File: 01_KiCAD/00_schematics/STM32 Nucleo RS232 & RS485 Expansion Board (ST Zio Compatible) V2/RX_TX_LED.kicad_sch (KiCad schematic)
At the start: 1 part

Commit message: Removed LED
LED verwijderd dat gebruikt werd voor GitHub Test
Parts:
- removed D1: LED, PCM_SparkFun-LED:LED_0603_1608Metric, symbol PCM_SparkFun-LED:LED
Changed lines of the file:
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@@
 		(comment 3 "Initial revision")
 	)
-	(symbol
-		(lib_id "PCM_SparkFun-LED:LED")
-		(at 73.66 67.31 90)
-		(unit 1)
-		(exclude_from_sim no)
-		(in_bom yes)
-		(on_board yes)
-		(dnp no)
-		(fields_autoplaced yes)
-		(property "Reference" "D1"
-			(at 76.2 65.9764 90)
-			(effects
-				(font
-					(size 1.27 1.27)
-				)
-				(justify right)
-			)
-		)
-		(property "Value" "LED"
-			(at 76.2 68.5164 90)
-			(effects
-				(font
-					(size 1.27 1.27)
-				)
-				(justify right)
-			)
-		)
-		(property "Footprint" "PCM_SparkFun-LED:LED_0603_1608Metric"
-			(at 78.74 67.31 0)
-			(effects
-				(font
-					(size 1.27 1.27)
-				)
-				(hide yes)
-			)
-		)
-		(property "Datasheet" "~"
-			(at 81.28 67.31 0)
-			(effects
-				(font
-					(size 1.27 1.27)
-				)
-				(hide yes)
-			)
-		)
-		(property "Description" "Light emitting diode"
-			(at 86.36 67.31 0)
-			(effects
-				(font
-					(size 1.27 1.27)
-				)
-				(hide yes)
-			)
-		)
-		(property "PROD_ID" "LED-"
-			(at 83.82 67.31 0)
-			(effects
-				(font
-					(size 1.27 1.27)
-				)
-				(hide yes)
-			)
-		)
-		(pin "1"
-		)
-		(pin "2"
-		)
-		(instances
-			(project ""
-				(path "/080f83b7-8913-48e8-ab8e-79cb12295542/d1bb9d55-41f4-4fc3-ae06-1adc98dc5d39"
-					(reference "D1")
-					(unit 1)
-				)
-			)
-		)
-	)
 )

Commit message: Added SHDN logic
Added the SHDN pin logic to have both hardware control and software control vor activating the THVD4431
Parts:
- added C10, C9: 100nF, PCM_SparkFun-Capacitor:C_0603_1608Metric, symbol PCM_SparkFun-Capacitor:0.1uF_0603_25V_20%
- added D2: 1N4148W, Diode_SMD:D_SOD-123, symbol Diode:1N4148W
- added R8: 1K, PCM_fab:R_0603, symbol PCM_fab:R_0603
- added R9: 100K, PCM_fab:R_0603, symbol PCM_fab:R_0603
- added U2: SN74LVC1G14DRL, Package_TO_SOT_SMD:SOT-553, symbol 74xGxx:SN74LVC1G14DRL
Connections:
- new net: D2.1 (K), R8.2
- new net GND: C10.2, C9.2, U2.3 (GND)
- new net L3-TXD: R8.1
- new net TX_RC: C10.1, C9.1, D2.2 (A), R9.2, U2.2
- new net VIO: R9.1

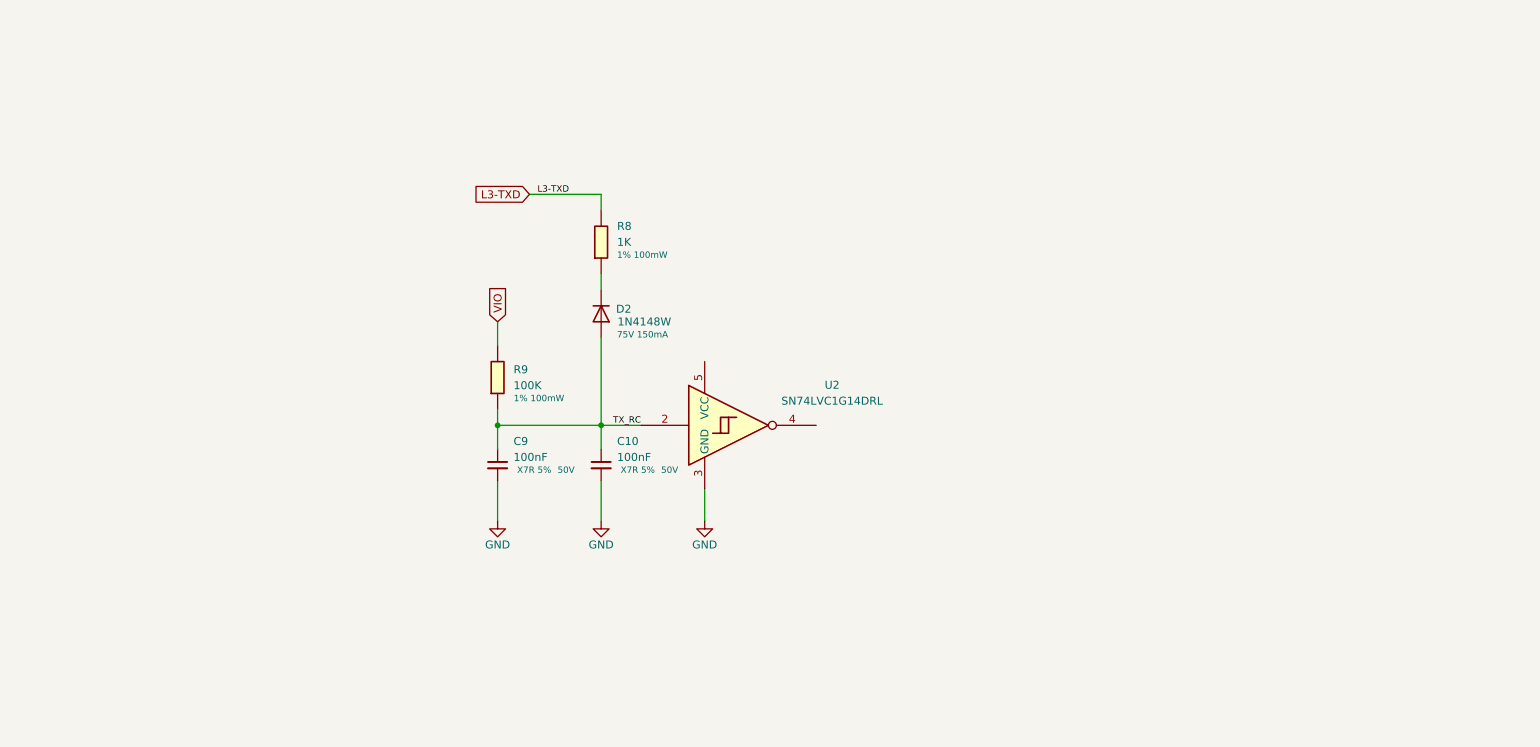
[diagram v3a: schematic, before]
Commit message: Added components and change device
Added dual Schmidt trigger input SN74LVC2G14DBV for LED Rx and Tx control.
Changed sn74hcs245 for alternate part sn74lvc245a for larger footprint and better availability with LCSC.
Difference is sn74lvc245a has no Schmidt-trigger inputs but instead just normal inputs. Fot details see dataseet. Both devices use exact same pin number and configuration except sn74lvc245a has no thermal pad or exposed pad like the sn74hcs245 has.
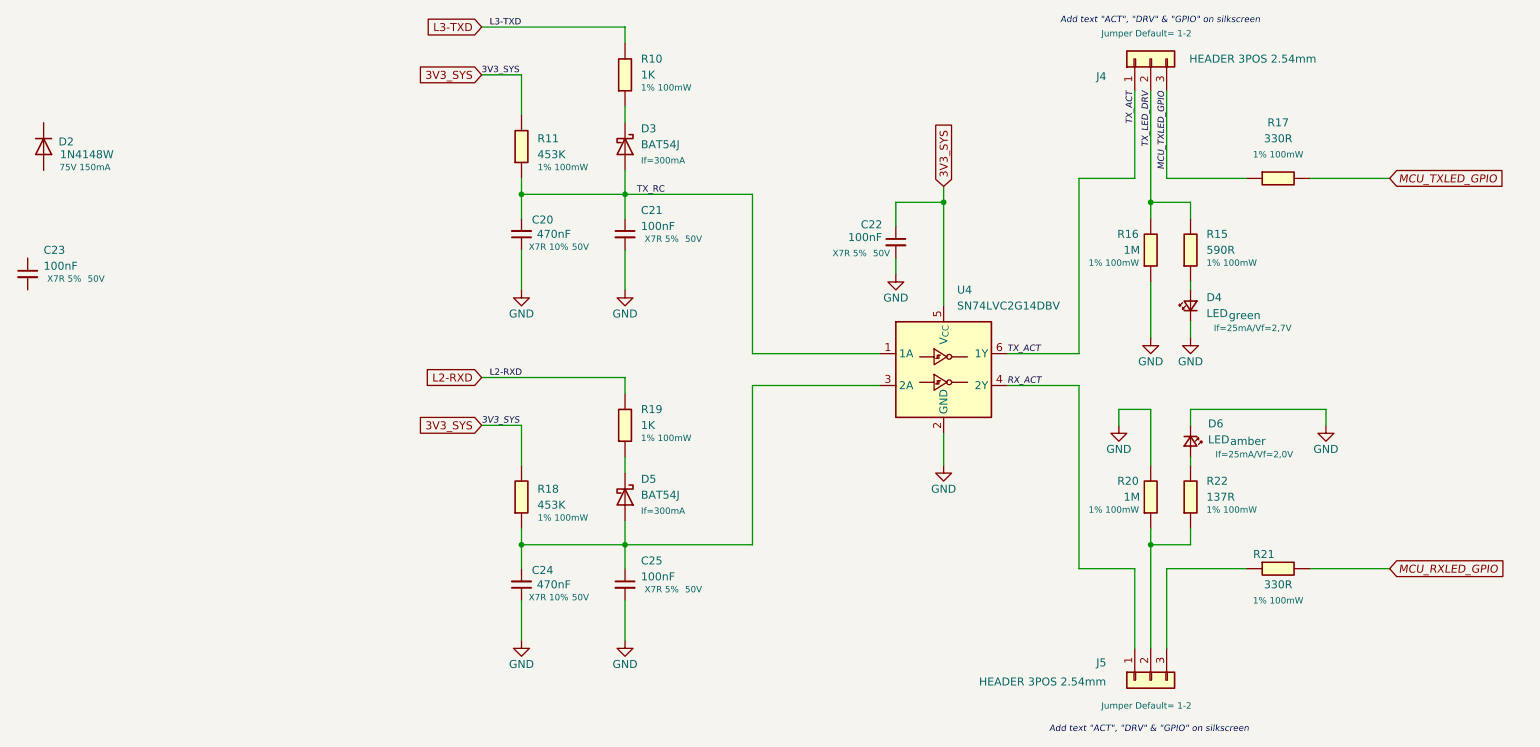
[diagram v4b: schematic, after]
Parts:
- removed U2: SN74LVC1G14DRL, Package_TO_SOT_SMD:SOT-553, symbol 74xGxx:SN74LVC1G14DRL
- added C20, C24: 470nF, PCM_SparkFun-Capacitor:C_0603_1608Metric, symbol PCM_SparkFun-Capacitor:0.1uF_0603_25V_20%
- added C22, C25: 100nF, PCM_SparkFun-Capacitor:C_0603_1608Metric, symbol PCM_SparkFun-Capacitor:0.1uF_0603_25V_20%
- added D3, D5: BAT54J, Diode_SMD:D_SOD-323F, symbol Diode:BAT54J
- added D4, D6: LED, IN-S63AT:LED_0603_WRE, symbol PCM_SparkFun-LED:LED
- added J4, J5: HEADER 3POS 2.54mm, symbol Connector_Generic:Conn_01x03
- added R15: 590R, PCM_fab:R_0603, symbol PCM_fab:R_0603
- added R16, R20: 1M, PCM_fab:R_0603, symbol PCM_fab:R_0603
- added R17, R21: 330R, PCM_fab:R_0603, symbol PCM_fab:R_0603
- added R18: 453K, PCM_fab:R_0603, symbol PCM_fab:R_0603
- added R19: 1K, PCM_fab:R_0603, symbol PCM_fab:R_0603
- added R22: 137R, PCM_fab:R_0603, symbol PCM_fab:R_0603
- added U4: SN74LVC2G14DBV, Package_TO_SOT_SMD:SOT-23-6, symbol 74xGxx:SN74LVC2G14DBV
- R11: renamed from R9; value 100K -> 453K; LCSC C14675 -> C114660; MPN RC0603FR-07100KL -> RC0603FR-07150KL
- renumbered C10 to C21, C9 to C23, R8 to R10
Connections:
- net GND: now also C20.1, C22.2, C24.1, C25.2, D4.1 (K), D6.1 (K), R16.2, R20.1, U4.2 (GND); no longer C23.2
- net TX_RC: now also C20.2, D3.2 (A), U4.1 (1A); no longer C23.1, D2.2 (A)
- net at R10.2: now also D3.1 (K); no longer D2.1 (K)
- net VIO renamed 3V3_SYS
- net 3V3_SYS: now also C22.1, R18.1, U4.5 (V_{CC})
- new net: J5.3 (Pin_3), R21.2
- new net: D5.1 (K), R19.2
- new net: D6.2 (A), R22.1
- new net: C24.2, C25.1, D5.2 (A), R18.2, U4.3 (2A)
- new net: D4.2 (A), R15.2
- new net: J5.2 (Pin_2), R20.2, R22.2
- new net L2-RXD: R19.1
- new net MCU_RXLED_GPIO: R21.1
- new net MCU_TXLED_GPIO: J4.3 (Pin_3), R17.1, R17.2
- new net RX_ACT: J5.1 (Pin_1), U4.4 (2Y)
- new net TX_ACT: J4.1 (Pin_1), U4.6 (1Y)
- new net TX_LED_DRV: J4.2 (Pin_2), R15.1, R16.1
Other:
- note added: "Add text "ACT", "DRV" & "GPIO" on silkscreen"
- moved on the sheet: C21, C23, D2, R10, R11

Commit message: Finisching touches to schematics
Finalizing the schematics and double-check all connections throughout the different sheets.
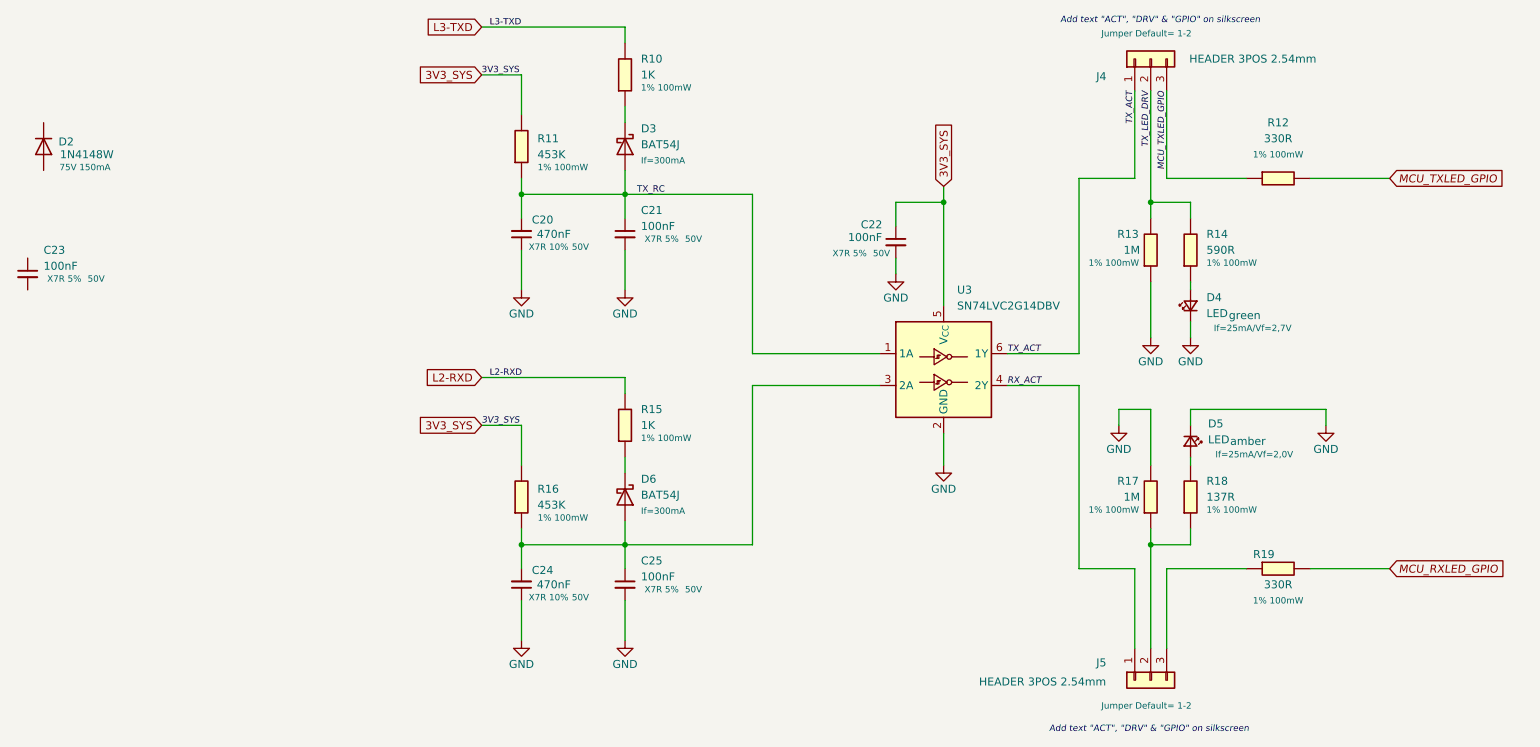
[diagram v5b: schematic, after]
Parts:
- renumbered D6 to D5, D5 to D6, R17 to R12, R16 to R13, R15 to R14, R19 to R15, R18 to R16, R20 to R17, R22 to R18, R21 to R19, U4 to U3
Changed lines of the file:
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@@
 		(on_board yes)
 		(dnp no)
-		(property "Reference" "R16"
+		(property "Reference" "R13"
 			(at 168.656 63.5 0)
 			(effects
@@
 			(project ""
 				(path "/080f83b7-8913-48e8-ab8e-79cb12295542/d1bb9d55-41f4-4fc3-ae06-1adc98dc5d39"
-					(reference "R16")
+					(reference "R13")
 					(unit 1)
 				)
@@
 		(on_board yes)
 		(dnp no)
-		(property "Reference" "R21"
+		(property "Reference" "R19"
 			(at 192.024 114.554 90)
 			(effects
@@
 			(project "STM32 Nucleo RS232 & RS485 Expansion Board (ST Zio Compatible) V2"
 				(path "/080f83b7-8913-48e8-ab8e-79cb12295542/d1bb9d55-41f4-4fc3-ae06-1adc98dc5d39"
-					(reference "R21")
+					(reference "R19")
 					(unit 1)
 				)
@@
 		(on_board yes)
 		(dnp no)
-		(property "Reference" "R19"
+		(property "Reference" "R15"
 			(at 92.71 91.4399 0)
 			(effects
@@
 			(project "STM32 Nucleo RS232 & RS485 Expansion Board (ST Zio Compatible) V2"
 				(path "/080f83b7-8913-48e8-ab8e-79cb12295542/d1bb9d55-41f4-4fc3-ae06-1adc98dc5d39"
-					(reference "R19")
+					(reference "R15")
 					(unit 1)
 				)
@@
 		(dnp no)
 		(fields_autoplaced yes)
-		(property "Reference" "#PWR027"
+		(property "Reference" "#PWR028"
 			(at 73.66 78.74 0)
 			(effects
@@
 			(project "STM32 Nucleo RS232 & RS485 Expansion Board (ST Zio Compatible) V2"
 				(path "/080f83b7-8913-48e8-ab8e-79cb12295542/d1bb9d55-41f4-4fc3-ae06-1adc98dc5d39"
-					(reference "#PWR027")
+					(reference "#PWR028")
 					(unit 1)
 				)
@@
 		(on_board yes)
 		(dnp no)
-		(property "Reference" "D6"
+		(property "Reference" "D5"
 			(at 183.134 93.726 90)
 			(effects
@@
 			(project "STM32 Nucleo RS232 & RS485 Expansion Board (ST Zio Compatible) V2"
 				(path "/080f83b7-8913-48e8-ab8e-79cb12295542/d1bb9d55-41f4-4fc3-ae06-1adc98dc5d39"
-					(reference "D6")
+					(reference "D5")
 					(unit 1)
 				)
@@
 		(dnp no)
 		(fields_autoplaced yes)
-		(property "Reference" "#PWR034"
+		(property "Reference" "#PWR035"
 			(at 73.66 134.62 0)
 			(effects
@@
 			(project "STM32 Nucleo RS232 & RS485 Expansion Board (ST Zio Compatible) V2"
 				(path "/080f83b7-8913-48e8-ab8e-79cb12295542/d1bb9d55-41f4-4fc3-ae06-1adc98dc5d39"
-					(reference "#PWR034")
+					(reference "#PWR035")
 					(unit 1)
 				)
@@
 		(dnp no)
 		(fields_autoplaced yes)
-		(property "Reference" "#PWR037"
+		(property "Reference" "#PWR033"
 			(at 201.93 100.33 0)
 			(effects
@@
 			(project "STM32 Nucleo RS232 & RS485 Expansion Board (ST Zio Compatible) V2"
 				(path "/080f83b7-8913-48e8-ab8e-79cb12295542/d1bb9d55-41f4-4fc3-ae06-1adc98dc5d39"
-					(reference "#PWR037")
+					(reference "#PWR033")
 					(unit 1)
 				)
@@
 		(dnp no)
 		(fields_autoplaced yes)
-		(property "Reference" "#PWR033"
+		(property "Reference" "#PWR030"
 			(at 173.99 86.36 0)
 			(effects
@@
 			(project "STM32 Nucleo RS232 & RS485 Expansion Board (ST Zio Compatible) V2"
 				(path "/080f83b7-8913-48e8-ab8e-79cb12295542/d1bb9d55-41f4-4fc3-ae06-1adc98dc5d39"
-					(reference "#PWR033")
+					(reference "#PWR030")
 					(unit 1)
 				)
@@
 		(dnp no)
 		(fields_autoplaced yes)
-		(property "Reference" "#PWR032"
+		(property "Reference" "#PWR031"
 			(at 180.34 86.36 0)
 			(effects
@@
 			(project "STM32 Nucleo RS232 & RS485 Expansion Board (ST Zio Compatible) V2"
 				(path "/080f83b7-8913-48e8-ab8e-79cb12295542/d1bb9d55-41f4-4fc3-ae06-1adc98dc5d39"
-					(reference "#PWR032")
+					(reference "#PWR031")
 					(unit 1)
 				)
@@
 		(on_board yes)
 		(dnp no)
-		(property "Reference" "R22"
+		(property "Reference" "R18"
 			(at 182.88 102.8699 0)
 			(effects
@@
 			(project "STM32 Nucleo RS232 & RS485 Expansion Board (ST Zio Compatible) V2"
 				(path "/080f83b7-8913-48e8-ab8e-79cb12295542/d1bb9d55-41f4-4fc3-ae06-1adc98dc5d39"
-					(reference "R22")
+					(reference "R18")
 					(unit 1)
 				)
@@
 		(dnp no)
 		(fields_autoplaced yes)
-		(property "Reference" "U4"
+		(property "Reference" "U3"
 			(at 143.1133 72.39 0)
 			(effects
@@
 			(project ""
 				(path "/080f83b7-8913-48e8-ab8e-79cb12295542/d1bb9d55-41f4-4fc3-ae06-1adc98dc5d39"
-					(reference "U4")
+					(reference "U3")
 					(unit 1)
 				)
@@
 		(dnp no)
 		(fields_autoplaced yes)
-		(property "Reference" "#PWR028"
+		(property "Reference" "#PWR029"
 			(at 90.17 78.74 0)
 			(effects
@@
 			(project "STM32 Nucleo RS232 & RS485 Expansion Board (ST Zio Compatible) V2"
 				(path "/080f83b7-8913-48e8-ab8e-79cb12295542/d1bb9d55-41f4-4fc3-ae06-1adc98dc5d39"
-					(reference "#PWR028")
+					(reference "#PWR029")
 					(unit 1)
 				)
@@
 		(dnp no)
 		(fields_autoplaced yes)
-		(property "Reference" "#PWR035"
+		(property "Reference" "#PWR036"
 			(at 90.17 134.62 0)
 			(effects
@@
 			(project "STM32 Nucleo RS232 & RS485 Expansion Board (ST Zio Compatible) V2"
 				(path "/080f83b7-8913-48e8-ab8e-79cb12295542/d1bb9d55-41f4-4fc3-ae06-1adc98dc5d39"
-					(reference "#PWR035")
+					(reference "#PWR036")
 					(unit 1)
 				)
@@
 		(dnp no)
 		(fields_autoplaced yes)
-		(property "Reference" "#PWR031"
+		(property "Reference" "#PWR034"
 			(at 140.97 106.68 0)
 			(effects
@@
 			(project "STM32 Nucleo RS232 & RS485 Expansion Board (ST Zio Compatible) V2"
 				(path "/080f83b7-8913-48e8-ab8e-79cb12295542/d1bb9d55-41f4-4fc3-ae06-1adc98dc5d39"
-					(reference "#PWR031")
+					(reference "#PWR034")
 					(unit 1)
 				)
@@
 		(on_board yes)
 		(dnp no)
-		(property "Reference" "R20"
+		(property "Reference" "R17"
 			(at 168.656 102.87 0)
 			(effects
@@
 			(project "STM32 Nucleo RS232 & RS485 Expansion Board (ST Zio Compatible) V2"
 				(path "/080f83b7-8913-48e8-ab8e-79cb12295542/d1bb9d55-41f4-4fc3-ae06-1adc98dc5d39"
-					(reference "R20")
+					(reference "R17")
 					(unit 1)
 				)
@@
 		(dnp no)
 		(fields_autoplaced yes)
-		(property "Reference" "R17"
+		(property "Reference" "R12"
 			(at 194.31 45.72 90)
 			(effects
@@
 			(project "STM32 Nucleo RS232 & RS485 Expansion Board (ST Zio Compatible) V2"
 				(path "/080f83b7-8913-48e8-ab8e-79cb12295542/d1bb9d55-41f4-4fc3-ae06-1adc98dc5d39"
-					(reference "R17")
+					(reference "R12")
 					(unit 1)
 				)
@@
 		(dnp no)
 		(fields_autoplaced yes)
-		(property "Reference" "#PWR036"
+		(property "Reference" "#PWR032"
 			(at 168.91 100.33 0)
 			(effects
@@
 			(project "STM32 Nucleo RS232 & RS485 Expansion Board (ST Zio Compatible) V2"
 				(path "/080f83b7-8913-48e8-ab8e-79cb12295542/d1bb9d55-41f4-4fc3-ae06-1adc98dc5d39"
-					(reference "#PWR036")
+					(reference "#PWR032")
 					(unit 1)
 				)
@@
 		(on_board yes)
 		(dnp no)
-		(property "Reference" "R18"
+		(property "Reference" "R16"
 			(at 76.2 104.1399 0)
 			(effects
@@
 			(project "STM32 Nucleo RS232 & RS485 Expansion Board (ST Zio Compatible) V2"
 				(path "/080f83b7-8913-48e8-ab8e-79cb12295542/d1bb9d55-41f4-4fc3-ae06-1adc98dc5d39"
-					(reference "R18")
+					(reference "R16")
 					(unit 1)
 				)
@@
 		(on_board yes)
 		(dnp no)
-		(property "Reference" "R15"
+		(property "Reference" "R14"
 			(at 182.88 63.4999 0)
 			(effects
@@
 			(project "STM32 Nucleo RS232 & RS485 Expansion Board (ST Zio Compatible) V2"
 				(path "/080f83b7-8913-48e8-ab8e-79cb12295542/d1bb9d55-41f4-4fc3-ae06-1adc98dc5d39"
-					(reference "R15")
+					(reference "R14")
 					(unit 1)
 				)
@@
 		(dnp no)
 		(fields_autoplaced yes)
-		(property "Reference" "D5"
+		(property "Reference" "D6"
 			(at 92.71 102.5524 90)
 			(effects
@@
 			(project "STM32 Nucleo RS232 & RS485 Expansion Board (ST Zio Compatible) V2"
 				(path "/080f83b7-8913-48e8-ab8e-79cb12295542/d1bb9d55-41f4-4fc3-ae06-1adc98dc5d39"
-					(reference "D5")
+					(reference "D6")
 					(unit 1)
 				)
@@
 		(dnp no)
 		(fields_autoplaced yes)
-		(property "Reference" "#PWR029"
+		(property "Reference" "#PWR027"
 			(at 133.35 76.2 0)
 			(effects
@@
 			(project "STM32 Nucleo RS232 & RS485 Expansion Board (ST Zio Compatible) V2"
 				(path "/080f83b7-8913-48e8-ab8e-79cb12295542/d1bb9d55-41f4-4fc3-ae06-1adc98dc5d39"
-					(reference "#PWR029")
+					(reference "#PWR027")
 					(unit 1)
 				)
